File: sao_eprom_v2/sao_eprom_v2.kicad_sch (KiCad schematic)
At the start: 32 parts, among them J1 Conn_01x03, J2 USB_C_Receptacle_USB2.0, J3 sao_v2_addon_tht, U1 W25Q128JVS, U2 RP2040, U3 24LC00, X1 SX3M12.000M20F30TNN

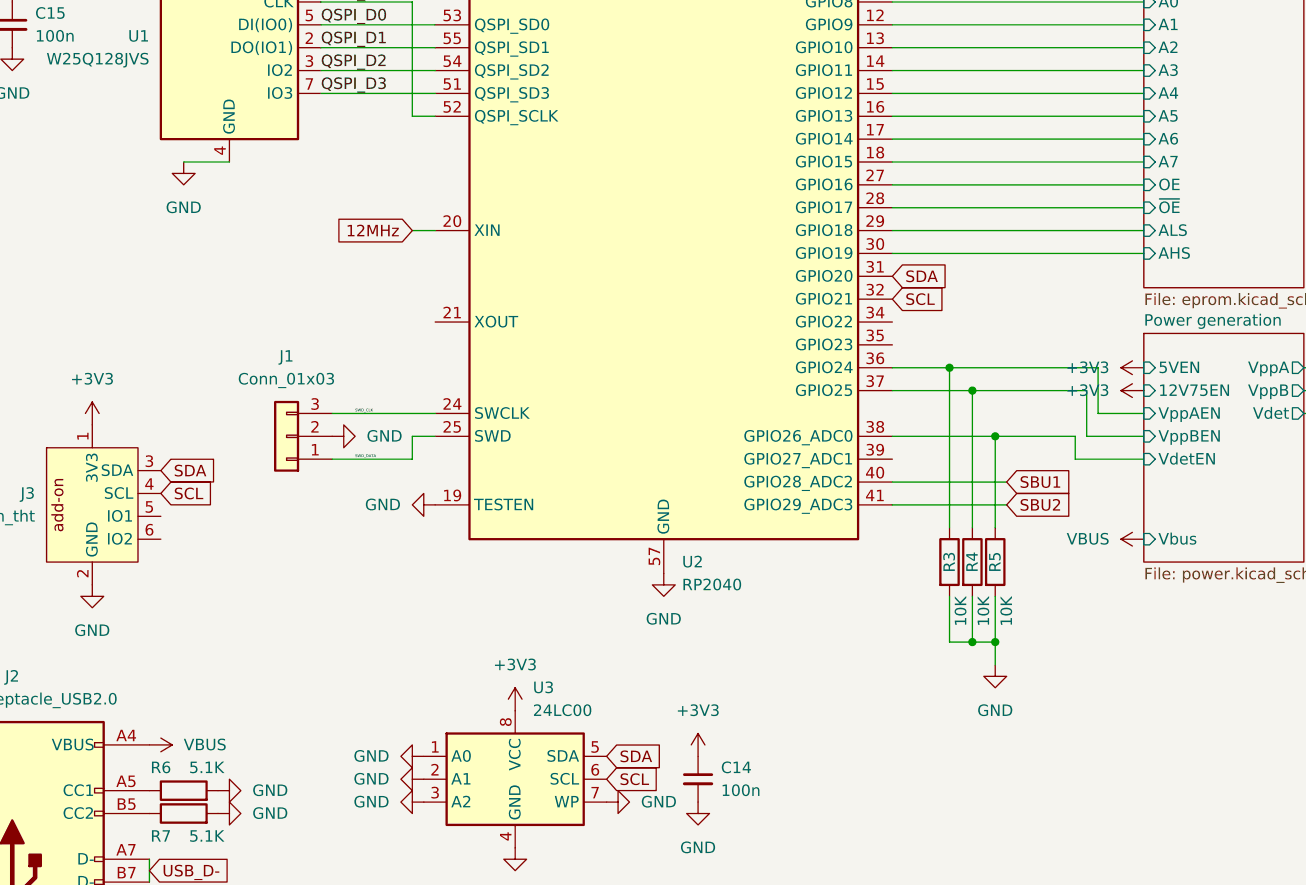
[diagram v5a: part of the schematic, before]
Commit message: Work some feedback into the schematic.
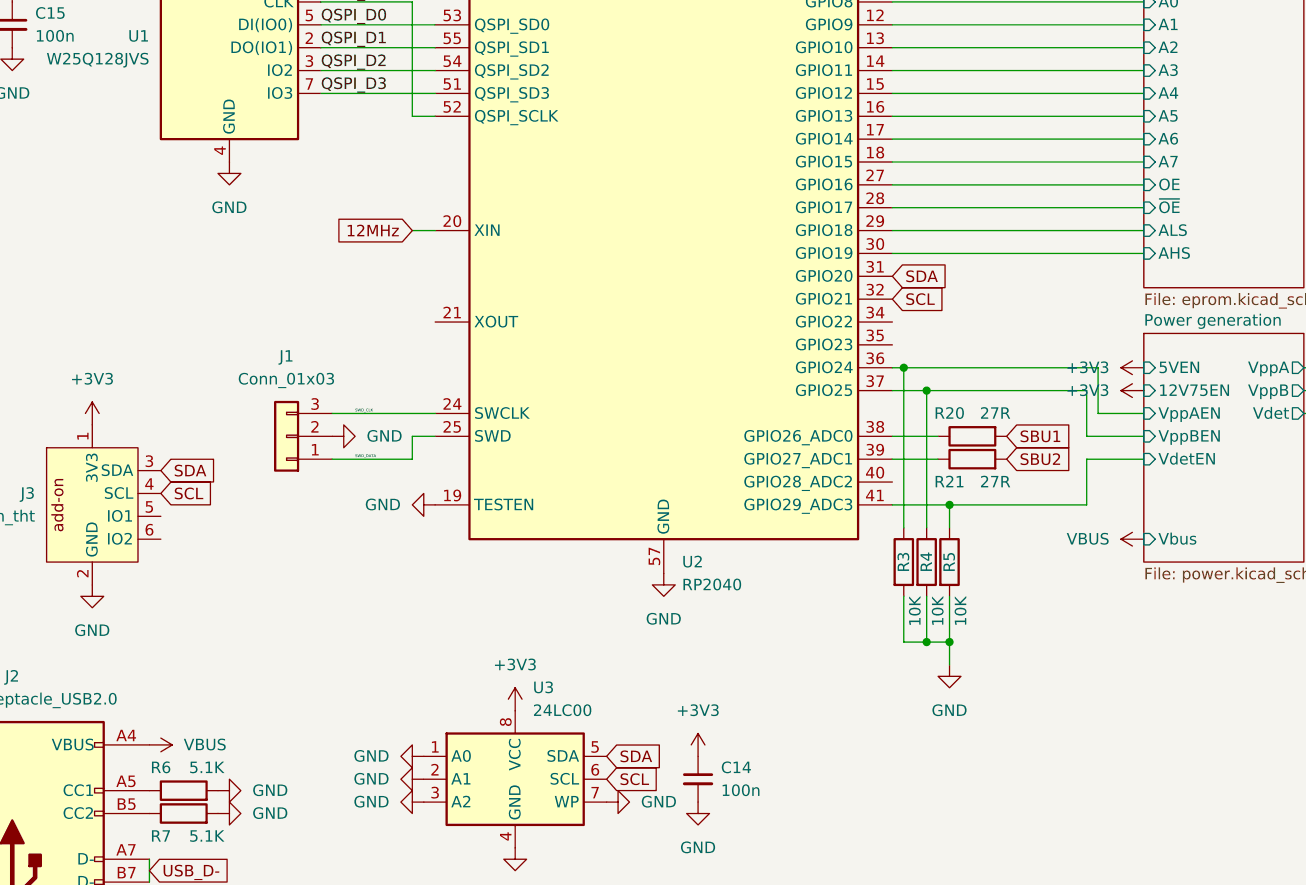
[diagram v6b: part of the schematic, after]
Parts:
- added R20, R21: 27R, Resistor_SMD:R_0402_1005Metric_Pad0.72x0.64mm_HandSolder, symbol Device:R
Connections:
- net Power generation/VdetEN: now also U2.41 (GPIO29_ADC3); no longer U2.38 (GPIO26_ADC0)
- net SBU1: now also R20.2; no longer U2.40 (GPIO28_ADC2)
- net SBU2: now also R21.2; no longer U2.41 (GPIO29_ADC3)
- net at U2.39 (GPIO27_ADC1): now also R21.1
- new net: R20.1, U2.38 (GPIO26_ADC0)
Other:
- moved on the sheet: R3, R4, R5

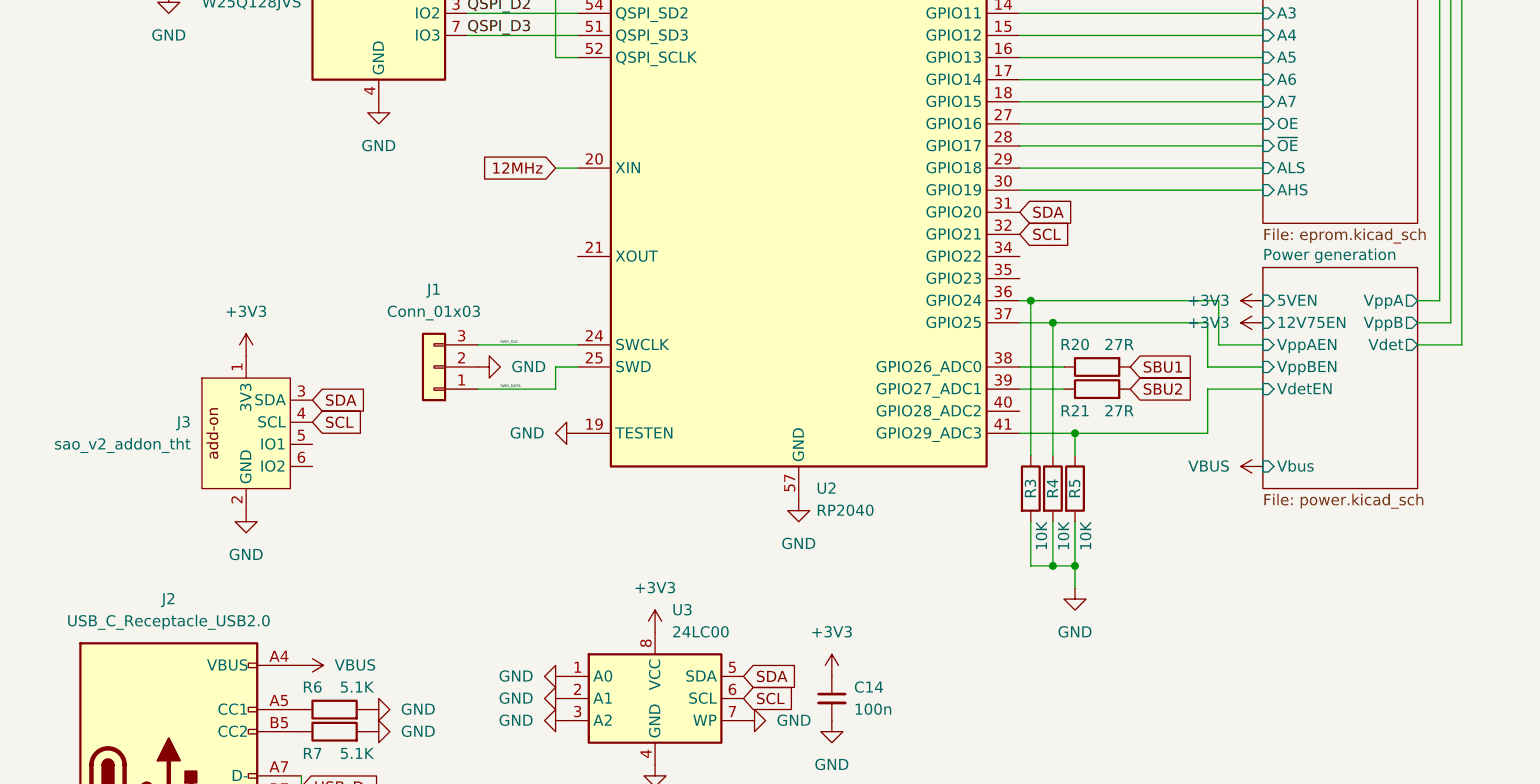
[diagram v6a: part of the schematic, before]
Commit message: Add some blinkenlights!
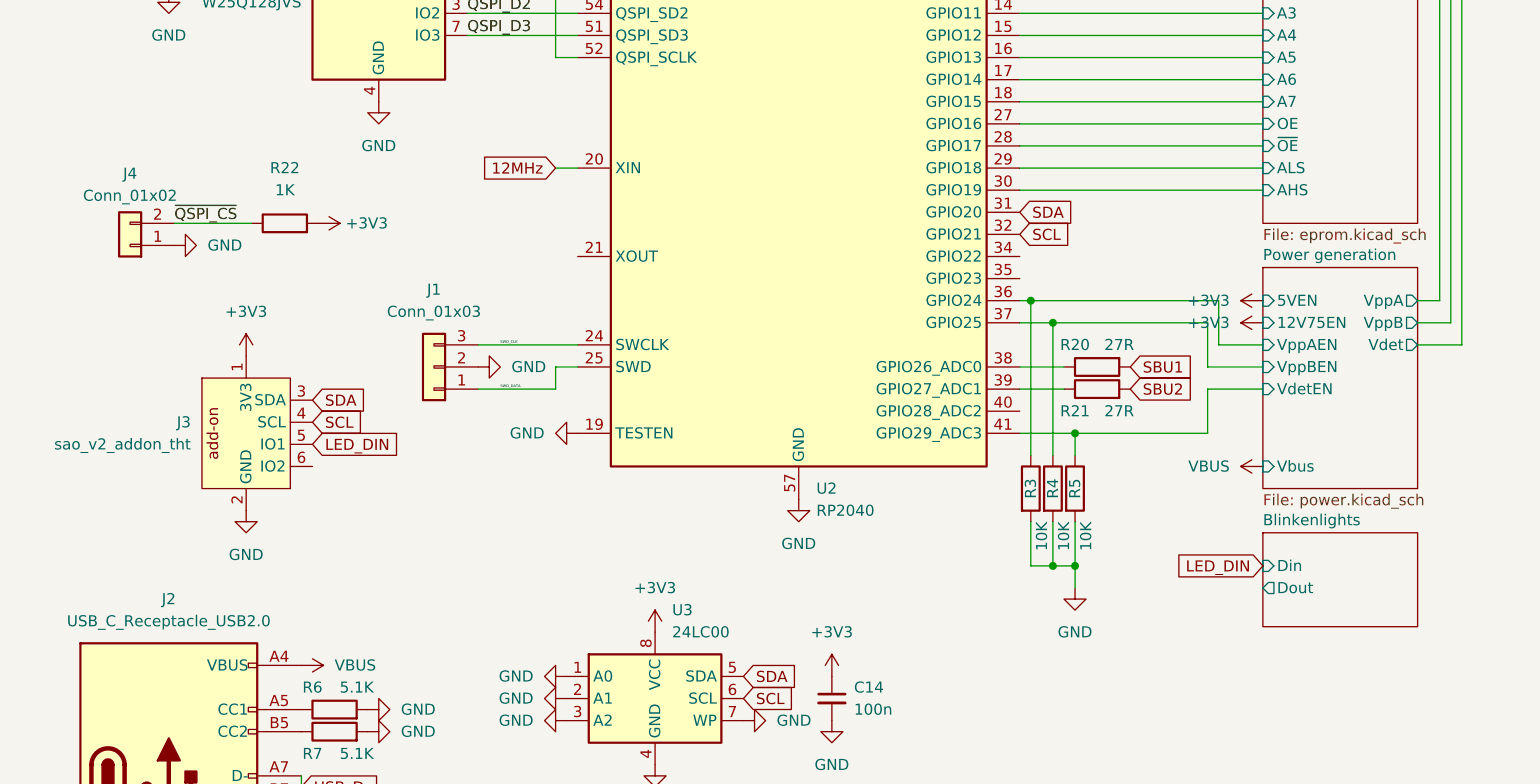
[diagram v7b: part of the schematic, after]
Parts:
- added J4: Conn_01x02, Connector_PinHeader_2.54mm:PinHeader_1x02_P2.54mm_Vertical, symbol Connector_Generic:Conn_01x02
- added R22: 1K, Resistor_SMD:R_0402_1005Metric_Pad0.72x0.64mm_HandSolder, symbol Device:R
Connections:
- net +3V3: now also R22.2
- net GND: now also J4.1 (Pin_1)
- net ~{QSPI_CS}: now also J4.2 (Pin_2), R22.1
- net LED_DIN: now reaches J3.5 (IO1)
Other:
- added sheet Blinkenlights (blinkenlights.kicad_sch)
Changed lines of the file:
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@@
+    (stroke (width 0) (type default))
+  )
+  (wire (pts (xy 31.115 93.98) (xy 40.005 93.98))
     (stroke (width 0) (type default))
   )
@@
   )
   (label "QSPI_D0" (at 64.77 64.77 0) (fields_autoplaced)
+    (effects (font (size 1.27 1.27)) (justify left bottom))
+  )
+  (label "~{QSPI_CS}" (at 31.115 93.98 0) (fields_autoplaced)
     (effects (font (size 1.27 1.27)) (justify left bottom))
   )
@@
     (property "Intersheetrefs" "${INTERSHEET_REFS}" (at 56.2458 158.75 0)
       (effects (font (size 1.27 1.27)) (justify left) hide)
+    )
+  )
+  (global_label "LED_DIN" (shape input) (at 46.99 119.38 0) (fields_autoplaced)
+    (effects (font (size 1.27 1.27)) (justify left))
+    (property "Intersheetrefs" "${INTERSHEET_REFS}" (at 57.5158 119.38 0)
+      (effects (font (size 1.27 1.27)) (justify left) hide)
+    )
+  )
+  (global_label "LED_DIN" (shape input) (at 156.21 133.35 180) (fields_autoplaced)
+    (effects (font (size 1.27 1.27)) (justify right))
+    (property "Intersheetrefs" "${INTERSHEET_REFS}" (at 145.6842 133.35 0)
+      (effects (font (size 1.27 1.27)) (justify right) hide)
     )
   )
@@
     )
   )
+  (symbol (lib_id "Connector_Generic:Conn_01x02") (at 26.035 96.52 180) (unit 1)
+    (in_bom yes) (on_board yes) (dnp no) (fields_autoplaced)
+    (property "Reference" "J4" (at 26.035 88.265 0)
+      (effects (font (size 1.27 1.27)))
+    )
+    (property "Value" "Conn_01x02" (at 26.035 90.805 0)
+      (effects (font (size 1.27 1.27)))
+    )
+    (property "Footprint" "Connector_PinHeader_2.54mm:PinHeader_1x02_P2.54mm_Vertical" (at 26.035 96.52 0)
+      (effects (font (size 1.27 1.27)) hide)
+    )
+    (property "Datasheet" "~" (at 26.035 96.52 0)
+      (effects (font (size 1.27 1.27)) hide)
+    )
+    (pin "1")
+    (pin "2")
+    (instances
+      (project "sao_eprom_v2"
+        (path "/07beccdd-32b3-4f03-aa51-fb5544b6f2d4"
+          (reference "J4") (unit 1)
+        )
+      )
+    )
+  )
   (symbol (lib_id "Device:R") (at 129.54 124.46 0) (unit 1)
     (in_bom yes) (on_board yes) (dnp no)
@@
     )
   )
+  (symbol (lib_id "power:GND") (at 31.115 96.52 90) (unit 1)
+    (in_bom yes) (on_board yes) (dnp no) (fields_autoplaced)
+    (property "Reference" "#PWR0106" (at 37.465 96.52 0)
+      (effects (font (size 1.27 1.27)) hide)
+    )
+    (property "Value" "GND" (at 34.925 96.52 90)
+      (effects (font (size 1.27 1.27)) (justify right))
+    )
+    (property "Footprint" "" (at 31.115 96.52 0)
+      (effects (font (size 1.27 1.27)) hide)
+    )
+    (property "Datasheet" "" (at 31.115 96.52 0)
+      (effects (font (size 1.27 1.27)) hide)
+    )
+    (pin "1")
+    (instances
+      (project "sao_eprom_v2"
+        (path "/07beccdd-32b3-4f03-aa51-fb5544b6f2d4"
+          (reference "#PWR0106") (unit 1)
+        )
+      )
+    )
+  )
   (symbol (lib_id "power:+3V3") (at 106.68 146.05 0) (unit 1)
     (in_bom yes) (on_board yes) (dnp no) (fields_autoplaced)
@@
         (path "/07beccdd-32b3-4f03-aa51-fb5544b6f2d4"
           (reference "X1") (unit 1)
+        )
+      )
+    )
+  )
+  (symbol (lib_id "Device:R") (at 43.815 93.98 90) (unit 1)
+    (in_bom yes) (on_board yes) (dnp no) (fields_autoplaced)
+    (property "Reference" "R22" (at 43.815 87.63 90)
+      (effects (font (size 1.27 1.27)))
+    )
+    (property "Value" "1K" (at 43.815 90.17 90)
+      (effects (font (size 1.27 1.27)))
+    )
+    (property "Footprint" "Resistor_SMD:R_0402_1005Metric_Pad0.72x0.64mm_HandSolder" (at 43.815 95.758 90)
+      (effects (font (size 1.27 1.27)) hide)
+    )
+    (property "Datasheet" "~" (at 43.815 93.98 0)
+      (effects (font (size 1.27 1.27)) hide)
+    )
+    (pin "1")
+    (pin "2")
+    (instances
+      (project "sao_eprom_v2"
+        (path "/07beccdd-32b3-4f03-aa51-fb5544b6f2d4"
+          (reference "R22") (unit 1)
         )
       )
@@
         (path "/07beccdd-32b3-4f03-aa51-fb5544b6f2d4"
           (reference "#PWR063") (unit 1)
+        )
+      )
+    )
+  )
+  (symbol (lib_id "power:+3V3") (at 47.625 93.98 270) (unit 1)
+    (in_bom yes) (on_board yes) (dnp no) (fields_autoplaced)
+    (property "Reference" "#PWR0107" (at 43.815 93.98 0)
+      (effects (font (size 1.27 1.27)) hide)
+    )
+    (property "Value" "+3V3" (at 50.8 93.98 90)
+      (effects (font (size 1.27 1.27)) (justify left))
+    )
+    (property "Footprint" "" (at 47.625 93.98 0)
+      (effects (font (size 1.27 1.27)) hide)
+    )
+    (property "Datasheet" "" (at 47.625 93.98 0)
+      (effects (font (size 1.27 1.27)) hide)
+    )
+    (pin "1")
+    (instances
+      (project "sao_eprom_v2"
+        (path "/07beccdd-32b3-4f03-aa51-fb5544b6f2d4"
+          (reference "#PWR0107") (unit 1)
         )
       )
@@
       )
     )
+  )
+  (sheet (at 156.21 129.54) (size 17.78 10.795) (fields_autoplaced)
+    (stroke (width 0.1524) (type solid))
+    (fill (color 0 0 0 0.0000))
+    (property "Sheetname" "Blinkenlights" (at 156.21 128.8284 0)
+      (effects (font (size 1.27 1.27)) (justify left bottom))
+    )
+    (property "Sheetfile" "blinkenlights.kicad_sch" (at 156.21 140.9196 0)
+      (effects (font (size 1.27 1.27)) (justify left top) hide)
+    )
+    (pin "Dout" output (at 156.21 135.89 180)
+      (effects (font (size 1.27 1.27)) (justify left))
+    )
+    (pin "Din" input (at 156.21 133.35 180)
+      (effects (font (size 1.27 1.27)) (justify left))
+    )
+    (instances
+      (project "sao_eprom_v2"
+        (path "/07beccdd-32b3-4f03-aa51-fb5544b6f2d4" (page "4"))
+      )
+    )
